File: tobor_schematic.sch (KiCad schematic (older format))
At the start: 22 parts, among them J1 Programmer, SW1 Bin detect right, SW2 Bin detect left, SW3 External RST, U1 LM7805_TO220, U10 TCRT5000, U2 LM7833_TO220, U3 LM7805_TO220, U4 TCRT5000, U5 TCRT5000

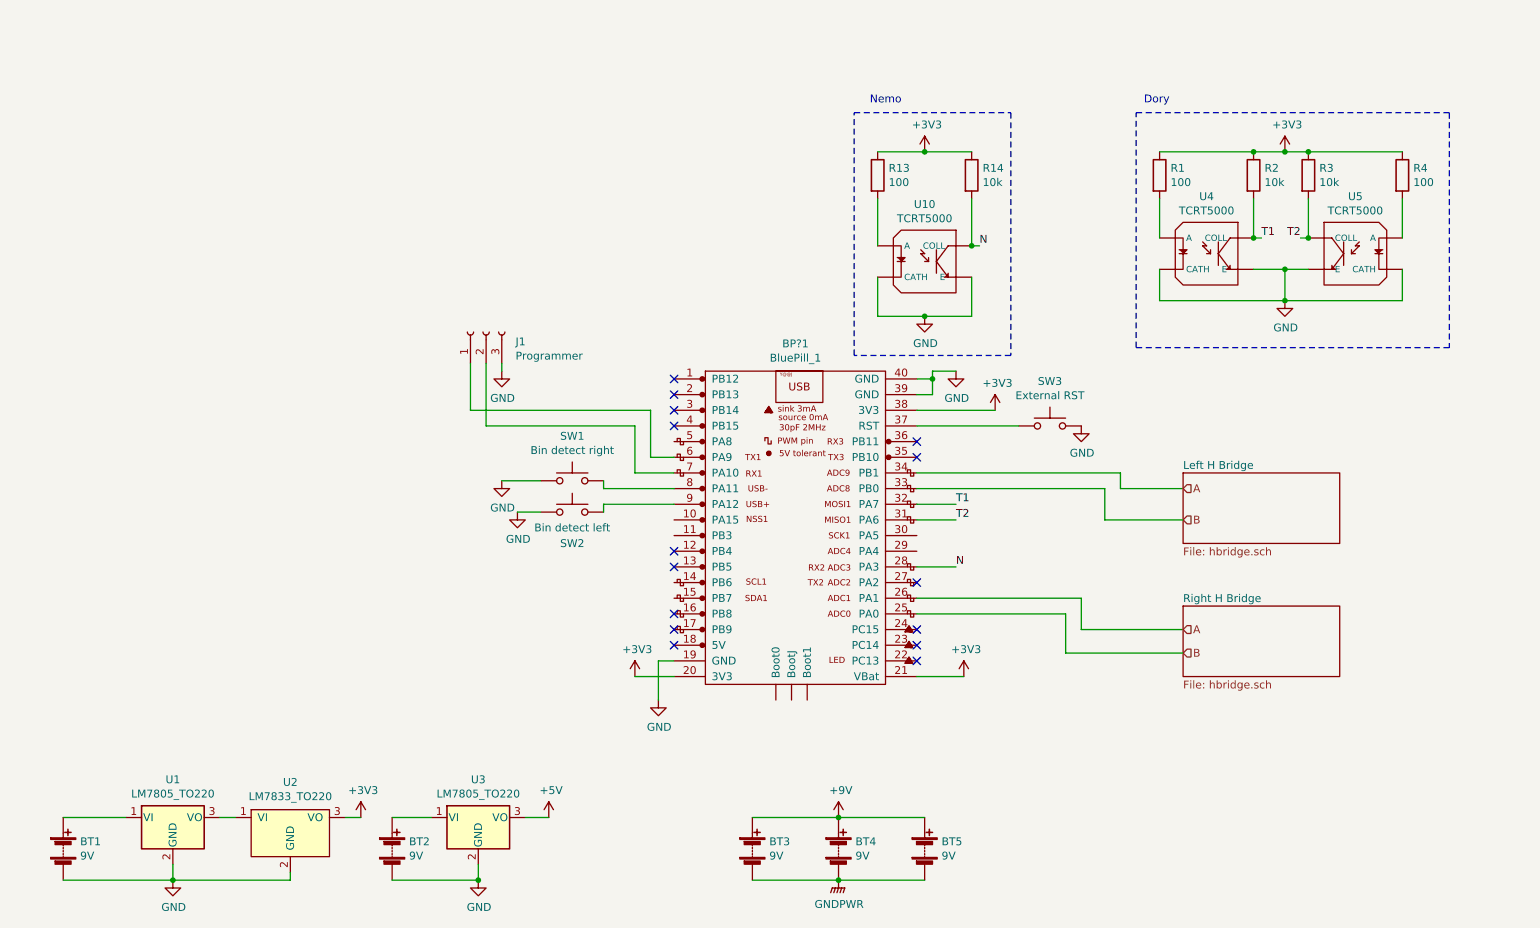
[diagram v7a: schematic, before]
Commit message: Add debug panel
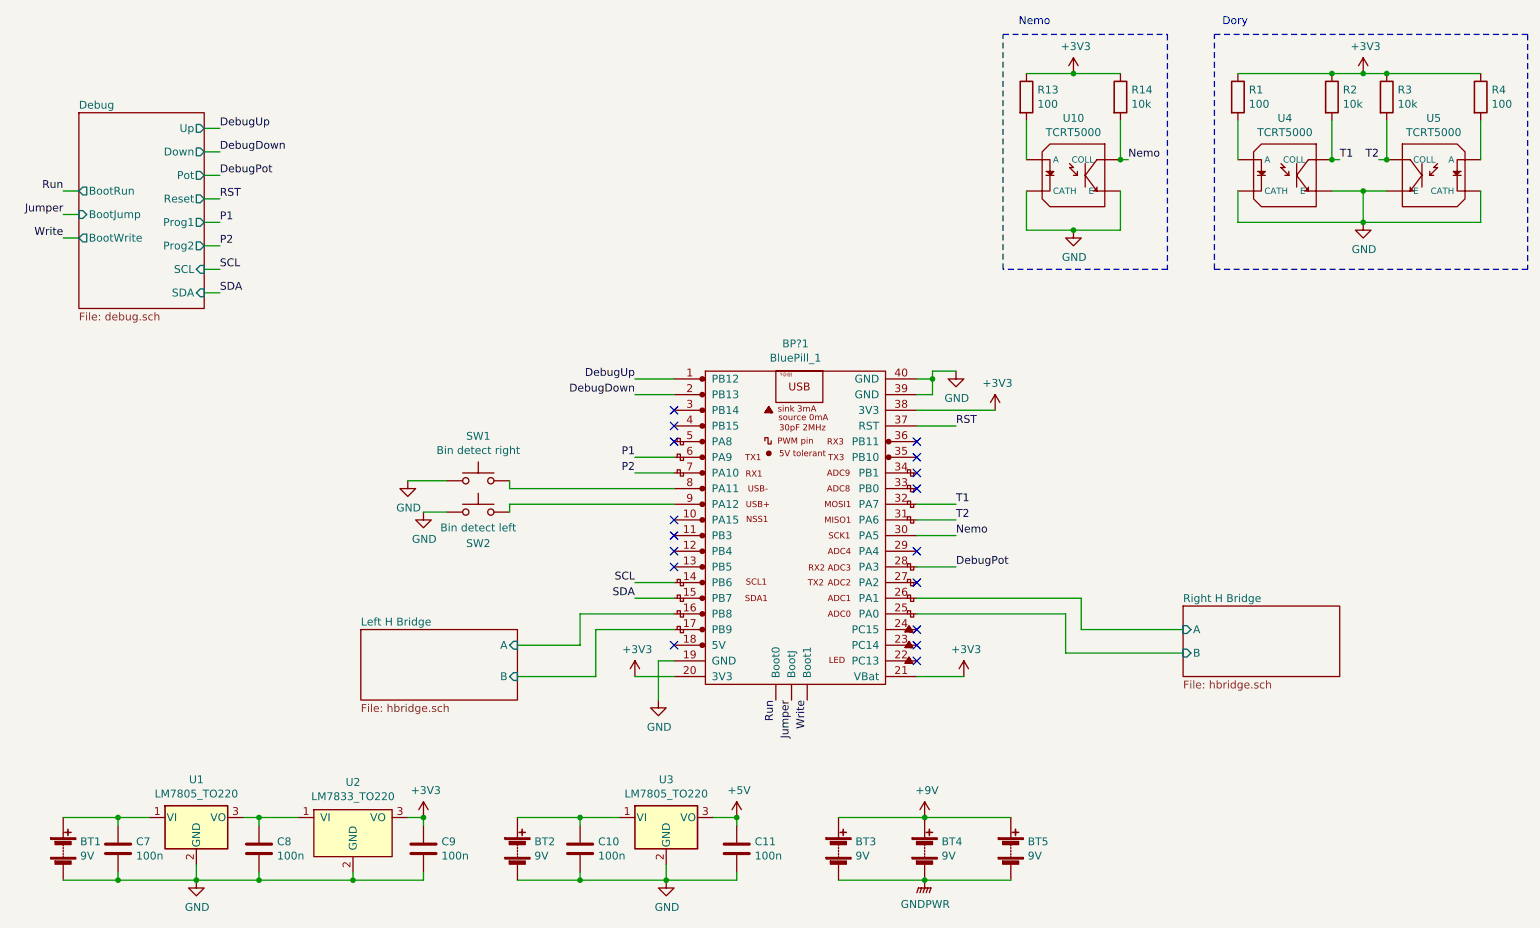
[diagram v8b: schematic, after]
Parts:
- removed J1: Programmer, symbol Connector:Conn_01x03_Female
- removed SW3: External RST, symbol Switch:SW_Push
- added C10, C11, C7, C8, C9: 100n, symbol Device:C
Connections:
- net +3V3: now also C9.1
- net +5V: now also C11.1
- net GND: now also C10.2, C11.2, C7.2, C8.2, C9.2
- net DebugUp: now reaches BP?1.1 (PB12)
- net SCL: now reaches BP?1.14 (PB6)
- net SDA: now reaches BP?1.15 (PB7)
- net Left H Bridge/A: now reaches BP?1.16 (PB8)
- net Left H Bridge/B: now reaches BP?1.17 (PB9)
- net DebugDown: now reaches BP?1.2 (PB13)
- net Nemo: now reaches BP?1.30 (PA5)
- net Nemo: now also R14.2, U10.C (COLL)
- net RST: now reaches BP?1.37 (RST)
- net P1: now reaches BP?1.6 (PA9)
- net P2: now reaches BP?1.7 (PA10)
- net Write: now reaches BP?1.~ (BootJ)
- net at BT1.1 (+), U1.1 (VI): now also C7.1
- net at BT2.1 (+), U3.1 (VI): now also C10.1
- net at U1.3 (VO), U2.1 (VI): now also C8.1
- net A: no longer names the net of BP?1.34 (PB1)
- net A: no longer BP?1.26 (PA1)
- net B: no longer names the net of BP?1.33 (PB0)
- net B: no longer BP?1.25 (PA0)
- removed net N: BP?1.28 (PA3), R14.2, U10.C (COLL)
- new net DebugPot: BP?1.28 (PA3)
- new net Jumper: BP?1.~ (BootJ)
- new net Right H Bridge/A: BP?1.26 (PA1)
- new net Right H Bridge/B: BP?1.25 (PA0)
- new net Run: BP?1.~ (BootJ)
- no-connect marks 15 -> 17
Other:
- moved on the sheet: BT2, BT3, BT4, BT5, R1, R13, R14, R2, R3, R4, SW1, SW2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
